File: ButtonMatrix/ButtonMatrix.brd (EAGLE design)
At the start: 44.5 x 67.3 mm, 10 parts

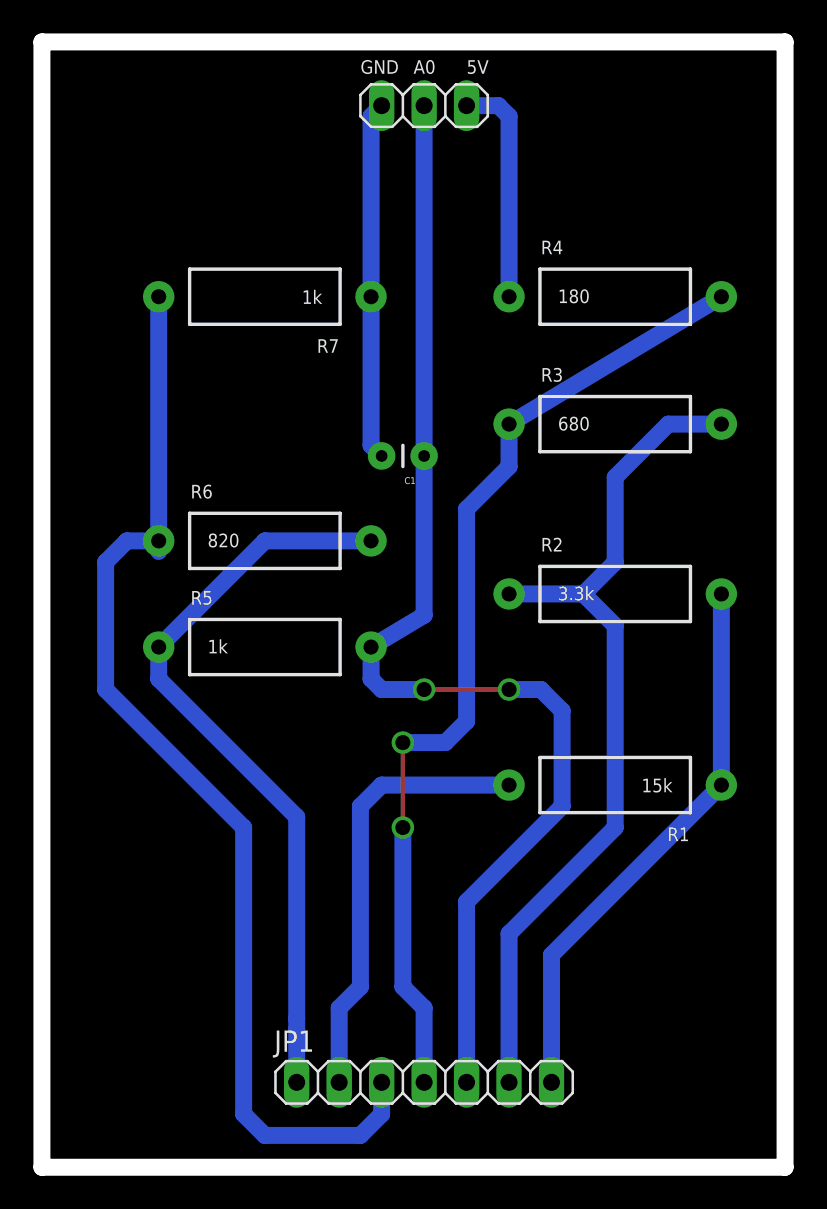
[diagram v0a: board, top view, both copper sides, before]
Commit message: remove old dead projects, add esp-01 sensor stuff
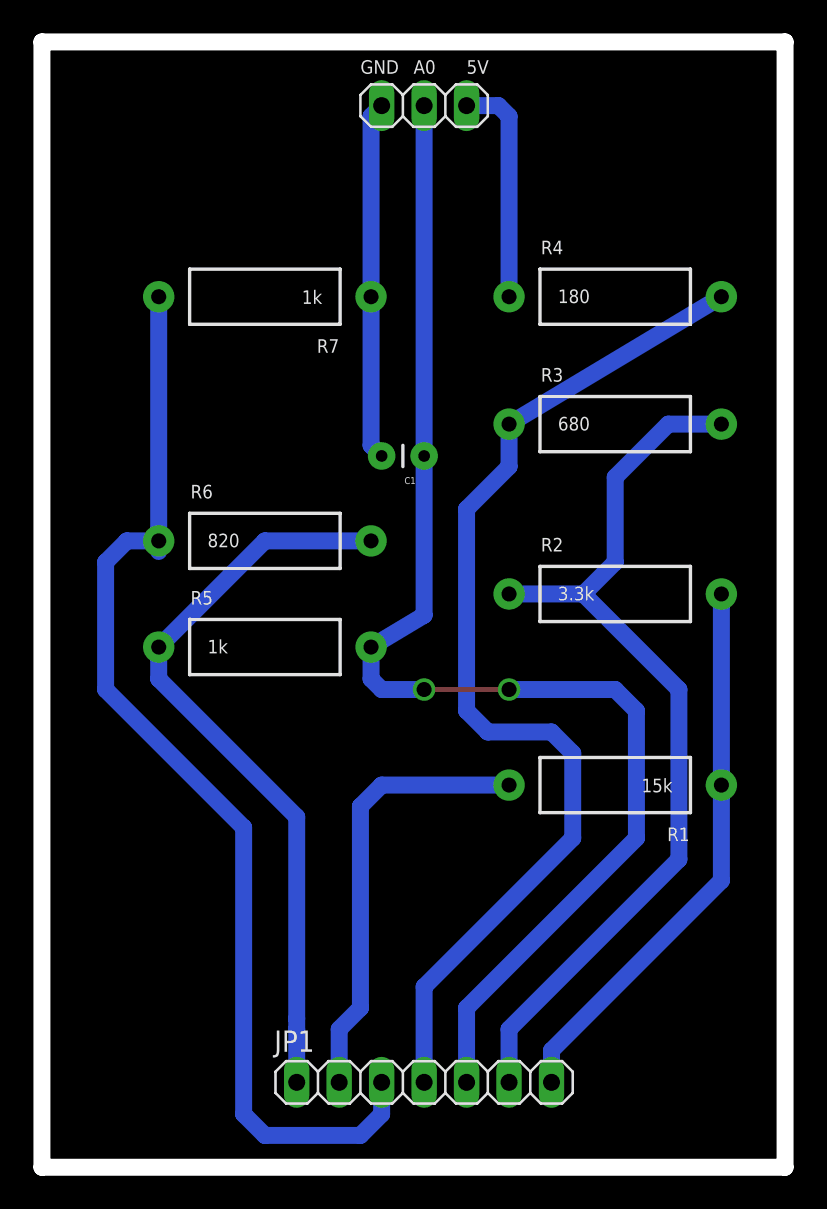
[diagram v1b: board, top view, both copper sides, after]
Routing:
- net A0: track 72.9 -> 79.2 mm
- net ROW*: track 58.8 -> 63.8 mm, vias 2 -> 0
- net ROW7: track 52.5 -> 55.7 mm
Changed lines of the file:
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@@
 <contactref element="JP1" pad="7"/>
 <wire x1="40.64" y1="22.86" x2="40.64" y2="34.29" width="1.016" layer="16"/>
-<wire x1="30.48" y1="4.445" x2="30.48" y2="12.7" width="0" layer="19" extent="1-16"/>
-<wire x1="30.48" y1="12.7" x2="40.64" y2="22.86" width="1.016" layer="16"/>
+<wire x1="30.48" y1="4.445" x2="30.48" y2="6.985" width="0" layer="19" extent="1-16"/>
+<wire x1="30.48" y1="6.985" x2="40.64" y2="22.86" width="0" layer="19" extent="1-16"/>
 <wire x1="30.48" y1="4.445" x2="30.48" y2="5.08" width="0" layer="19" extent="16-16"/>
-<wire x1="30.48" y1="12.7" x2="30.48" y2="5.08" width="1.016" layer="16"/>
+<wire x1="30.48" y1="6.985" x2="30.48" y2="5.08" width="1.016" layer="16"/>
+<wire x1="30.48" y1="6.985" x2="36.83" y2="13.335" width="0" layer="19" extent="1-16"/>
+<wire x1="36.195" y1="13.335" x2="40.005" y2="17.145" width="0" layer="19" extent="1-16"/>
+<wire x1="40.005" y1="17.145" x2="40.64" y2="17.145" width="0" layer="19" extent="1-16"/>
+<wire x1="40.64" y1="17.145" x2="40.64" y2="22.86" width="1.016" layer="16"/>
+<wire x1="30.48" y1="6.985" x2="40.64" y2="17.145" width="1.016" layer="16"/>
+<wire x1="36.195" y1="13.335" x2="36.83" y2="13.335" width="0" layer="19" extent="1-16"/>
 </signal>
 <signal name="ROW7">
@@
 <contactref element="R3" pad="P$2"/>
 <contactref element="JP1" pad="6"/>
-<wire x1="27.94" y1="5.08" x2="27.94" y2="13.97" width="1.016" layer="16"/>
-<wire x1="27.94" y1="13.97" x2="34.29" y2="20.32" width="1.016" layer="16"/>
-<wire x1="34.29" y1="20.32" x2="34.29" y2="32.385" width="1.016" layer="16"/>
-<wire x1="34.29" y1="32.385" x2="32.385" y2="34.29" width="1.016" layer="16"/>
+<wire x1="27.94" y1="5.08" x2="27.94" y2="8.255" width="1.016" layer="16"/>
+<wire x1="27.94" y1="10.795" x2="34.29" y2="20.32" width="0" layer="19" extent="1-16"/>
+<wire x1="34.29" y1="20.32" x2="34.29" y2="32.385" width="0" layer="19" extent="1-16"/>
+<wire x1="34.29" y1="32.385" x2="32.385" y2="34.29" width="0" layer="19" extent="1-16"/>
 <wire x1="32.385" y1="34.29" x2="27.94" y2="34.29" width="1.016" layer="16"/>
 <wire x1="32.385" y1="34.29" x2="34.29" y2="36.195" width="1.016" layer="16"/>
@@
 <wire x1="34.29" y1="41.275" x2="37.465" y2="44.45" width="1.016" layer="16"/>
 <wire x1="37.465" y1="44.45" x2="40.64" y2="44.45" width="1.016" layer="16"/>
+<wire x1="27.94" y1="10.795" x2="27.94" y2="8.255" width="0" layer="19" extent="1-16"/>
+<wire x1="27.94" y1="8.255" x2="38.1" y2="18.415" width="1.016" layer="16"/>
+<wire x1="38.1" y1="18.415" x2="38.1" y2="28.575" width="1.016" layer="16"/>
+<wire x1="38.1" y1="28.575" x2="32.385" y2="34.29" width="1.016" layer="16"/>
 </signal>
 <signal name="ROW*">
@@
 <contactref element="R4" pad="P$2"/>
 <contactref element="JP1" pad="4"/>
-<wire x1="21.59" y1="20.32" x2="21.59" y2="25.4" width="0.254" layer="1"/>
-<via x="21.59" y="20.32" extent="1-16" drill="0.9"/>
-<via x="21.59" y="25.4" extent="1-16" drill="0.9"/>
-<wire x1="25.4" y1="39.37" x2="25.4" y2="26.67" width="1.016" layer="16"/>
-<wire x1="21.59" y1="25.4" x2="24.13" y2="25.4" width="1.016" layer="16"/>
-<wire x1="22.86" y1="5.08" x2="22.86" y2="9.525" width="1.016" layer="16"/>
-<wire x1="22.86" y1="9.525" x2="21.59" y2="10.795" width="1.016" layer="16"/>
-<wire x1="21.59" y1="10.795" x2="21.59" y2="20.32" width="1.016" layer="16"/>
+<wire x1="25.4" y1="39.37" x2="25.4" y2="27.305" width="1.016" layer="16"/>
+<wire x1="22.86" y1="5.08" x2="22.86" y2="10.795" width="1.016" layer="16"/>
 <wire x1="27.94" y1="44.45" x2="40.64" y2="52.07" width="1.016" layer="16"/>
 <wire x1="25.4" y1="39.37" x2="27.94" y2="41.91" width="1.016" layer="16"/>
 <wire x1="27.94" y1="41.91" x2="27.94" y2="44.45" width="1.016" layer="16"/>
-<wire x1="24.13" y1="25.4" x2="25.4" y2="26.67" width="1.016" layer="16"/>
+<wire x1="25.4" y1="27.305" x2="26.67" y2="26.035" width="1.016" layer="16"/>
+<wire x1="26.67" y1="26.035" x2="30.48" y2="26.035" width="1.016" layer="16"/>
+<wire x1="30.48" y1="26.035" x2="31.75" y2="24.765" width="1.016" layer="16"/>
+<wire x1="31.75" y1="24.765" x2="31.75" y2="19.685" width="1.016" layer="16"/>
+<wire x1="31.75" y1="19.685" x2="22.86" y2="10.795" width="1.016" layer="16"/>
 </signal>
 <signal name="GND">
@@
 <wire x1="19.685" y1="29.21" x2="20.32" y2="28.575" width="1.016" layer="16"/>
 <wire x1="20.32" y1="28.575" x2="22.86" y2="28.575" width="1.016" layer="16"/>
-<wire x1="27.94" y1="28.575" x2="29.845" y2="28.575" width="1.016" layer="16"/>
-<wire x1="29.845" y1="28.575" x2="31.115" y2="27.305" width="1.016" layer="16"/>
-<wire x1="31.115" y1="27.305" x2="31.115" y2="21.59" width="1.016" layer="16"/>
-<wire x1="31.115" y1="21.59" x2="25.4" y2="15.875" width="1.016" layer="16"/>
-<wire x1="25.4" y1="15.875" x2="25.4" y2="5.08" width="1.016" layer="16"/>
+<wire x1="27.94" y1="28.575" x2="29.845" y2="28.575" width="0" layer="19" extent="1-16"/>
+<wire x1="29.845" y1="28.575" x2="31.115" y2="27.305" width="0" layer="19" extent="1-16"/>
+<wire x1="31.115" y1="27.305" x2="31.115" y2="21.59" width="0" layer="19" extent="1-16"/>
+<wire x1="31.115" y1="21.59" x2="25.4" y2="11.43" width="0" layer="19" extent="1-16"/>
+<wire x1="25.4" y1="9.525" x2="25.4" y2="5.08" width="1.016" layer="16"/>
+<wire x1="25.4" y1="11.43" x2="25.4" y2="9.525" width="0" layer="19" extent="1-16"/>
+<wire x1="25.4" y1="9.525" x2="35.56" y2="19.685" width="1.016" layer="16"/>
+<wire x1="35.56" y1="19.685" x2="35.56" y2="27.305" width="1.016" layer="16"/>
+<wire x1="35.56" y1="27.305" x2="34.29" y2="28.575" width="1.016" layer="16"/>
+<wire x1="34.29" y1="28.575" x2="27.94" y2="28.575" width="1.016" layer="16"/>
 </signal>
 <signal name="ROW1">
 <contactref element="JP1" pad="2"/>
-<wire x1="17.78" y1="9.525" x2="19.05" y2="10.795" width="1.016" layer="16"/>
+<wire x1="17.78" y1="8.255" x2="19.05" y2="9.525" width="1.016" layer="16"/>
 <contactref element="R1" pad="P$2"/>
 <wire x1="19.05" y1="21.59" x2="20.32" y2="22.86" width="1.016" layer="16"/>
 <wire x1="20.32" y1="22.86" x2="27.94" y2="22.86" width="1.016" layer="16"/>
-<wire x1="19.05" y1="10.795" x2="19.05" y2="21.59" width="1.016" layer="16"/>
-<wire x1="17.78" y1="9.525" x2="17.78" y2="5.08" width="1.016" layer="16"/>
+<wire x1="19.05" y1="9.525" x2="19.05" y2="21.59" width="1.016" layer="16"/>
+<wire x1="17.78" y1="8.255" x2="17.78" y2="5.08" width="1.016" layer="16"/>
 </signal>
 <signal name="5V">
